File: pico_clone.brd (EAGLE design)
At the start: 68.6 x 48.3 mm, 46 parts, among them IC1 RP2040-QFN56, Q1 12MHz, U1 W25Q128JVSIM

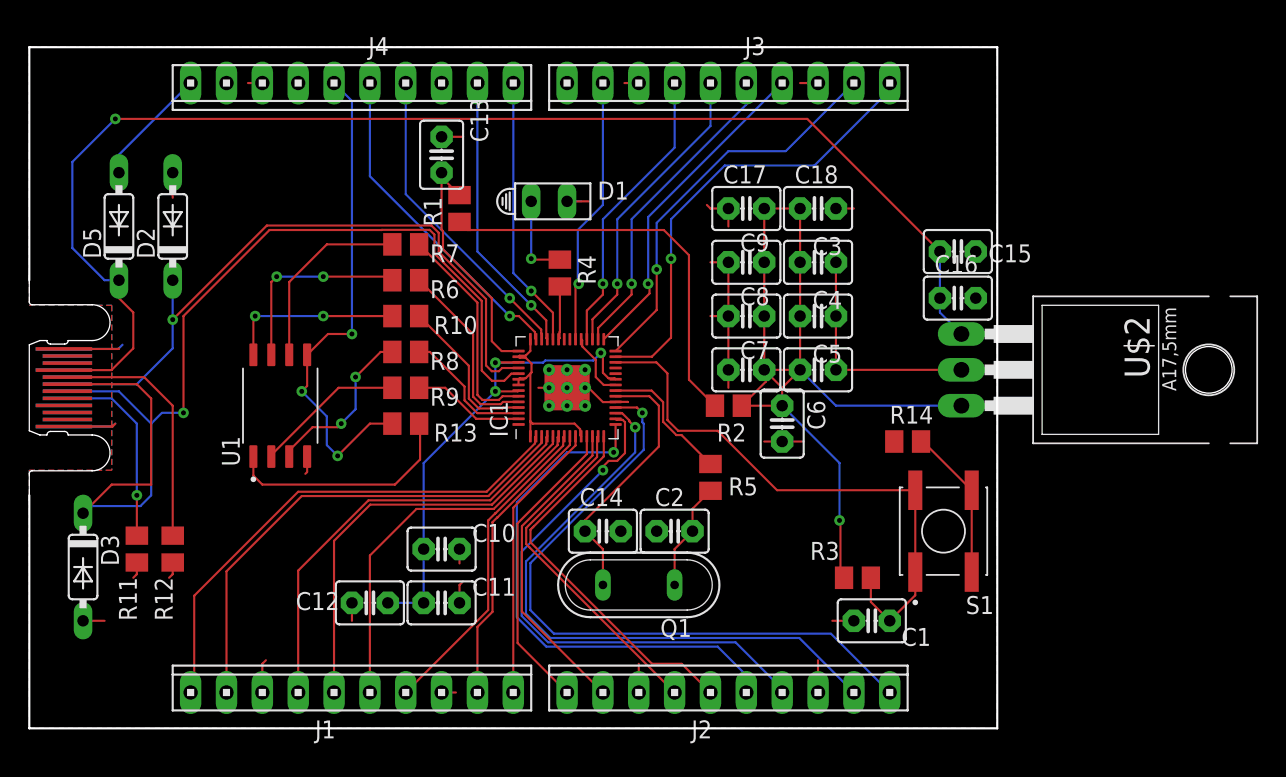
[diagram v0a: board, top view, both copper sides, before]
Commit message: update gnd & unmatchet pins
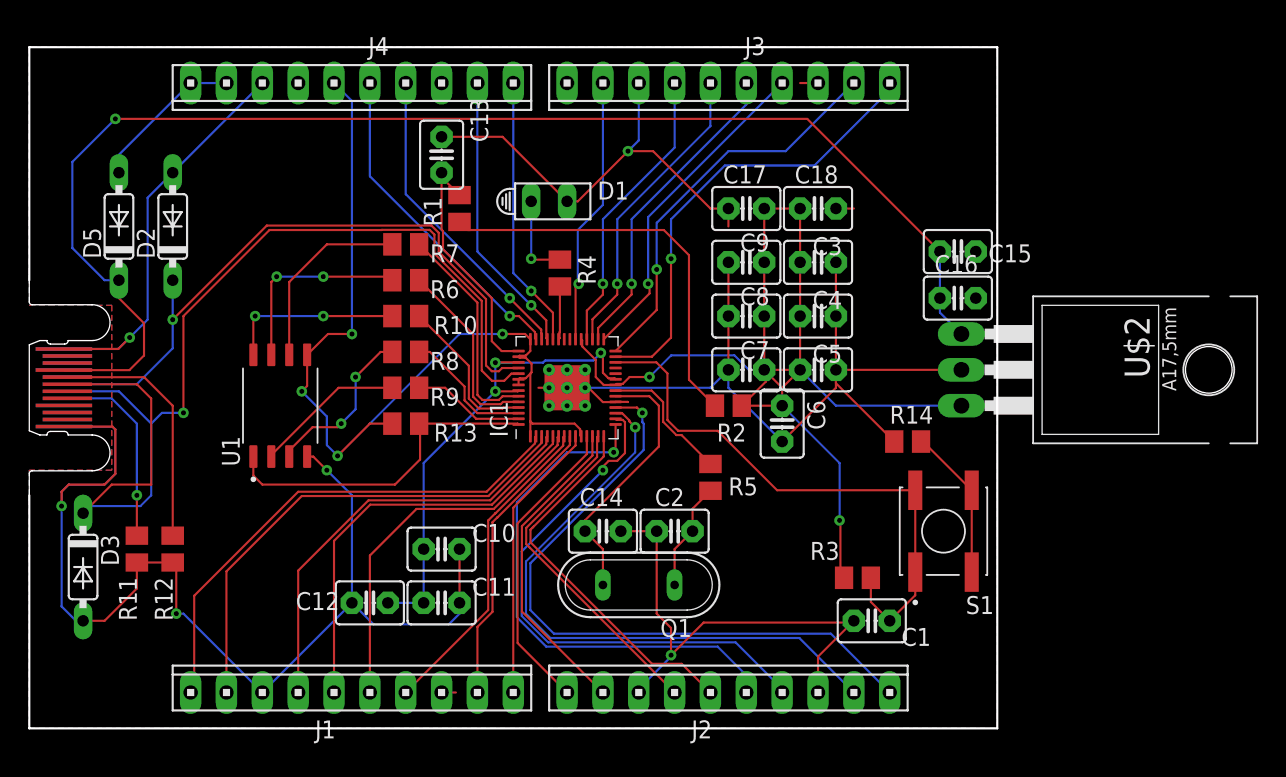
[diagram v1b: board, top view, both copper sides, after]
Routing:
- net GND: track 86.9 -> 255.5 mm, vias 0 -> 6
- net 3V3: track 119.1 -> 148.4 mm, vias 4 -> 6
- net QSPI_SS: track 16.7 -> 23.8 mm
- net N$14: track 94.2 -> 95.6 mm
- net VBUS: track 9.72 -> 11.0 mm
